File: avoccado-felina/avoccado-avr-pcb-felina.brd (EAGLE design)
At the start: 42.5 x 17.5 mm, 81 parts, among them Q1 16MHz, Q2 FET, U1 MPU-6000QFN-24, U2 MCP73831

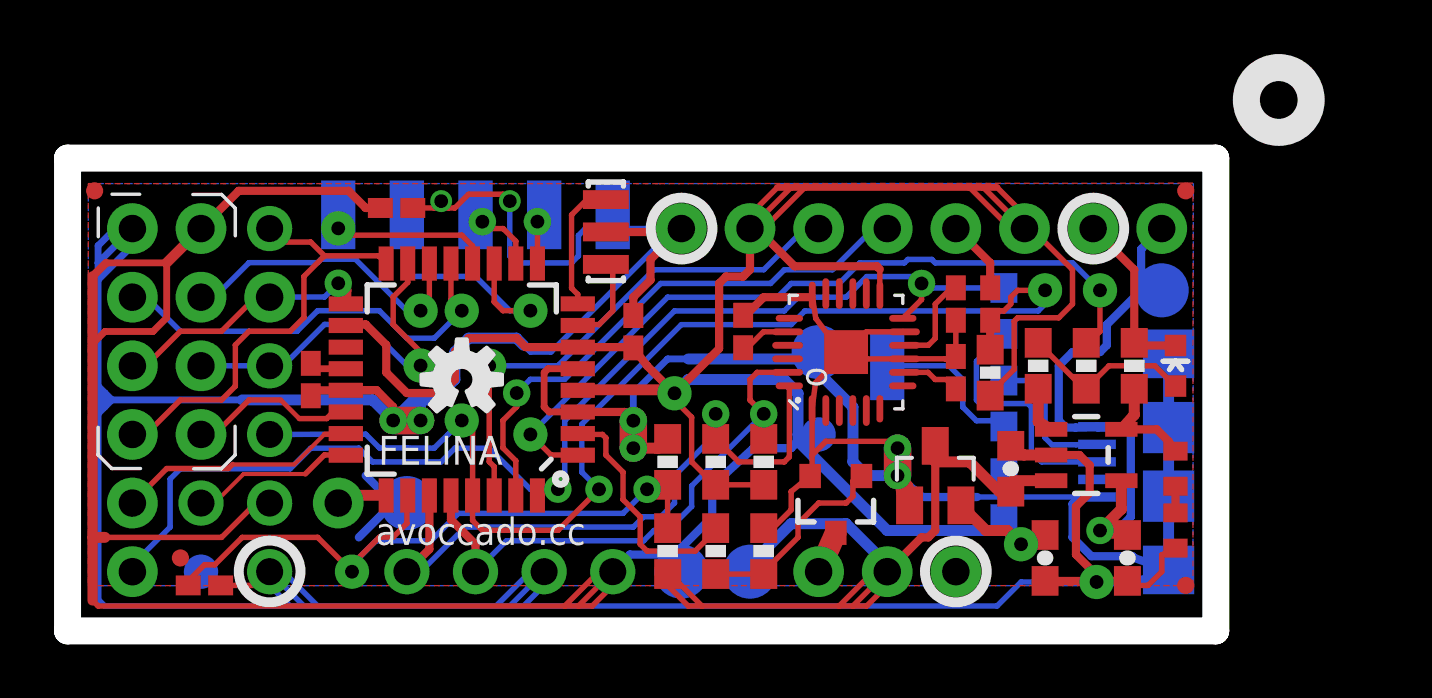
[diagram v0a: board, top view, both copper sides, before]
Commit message: rearrange board for panelization
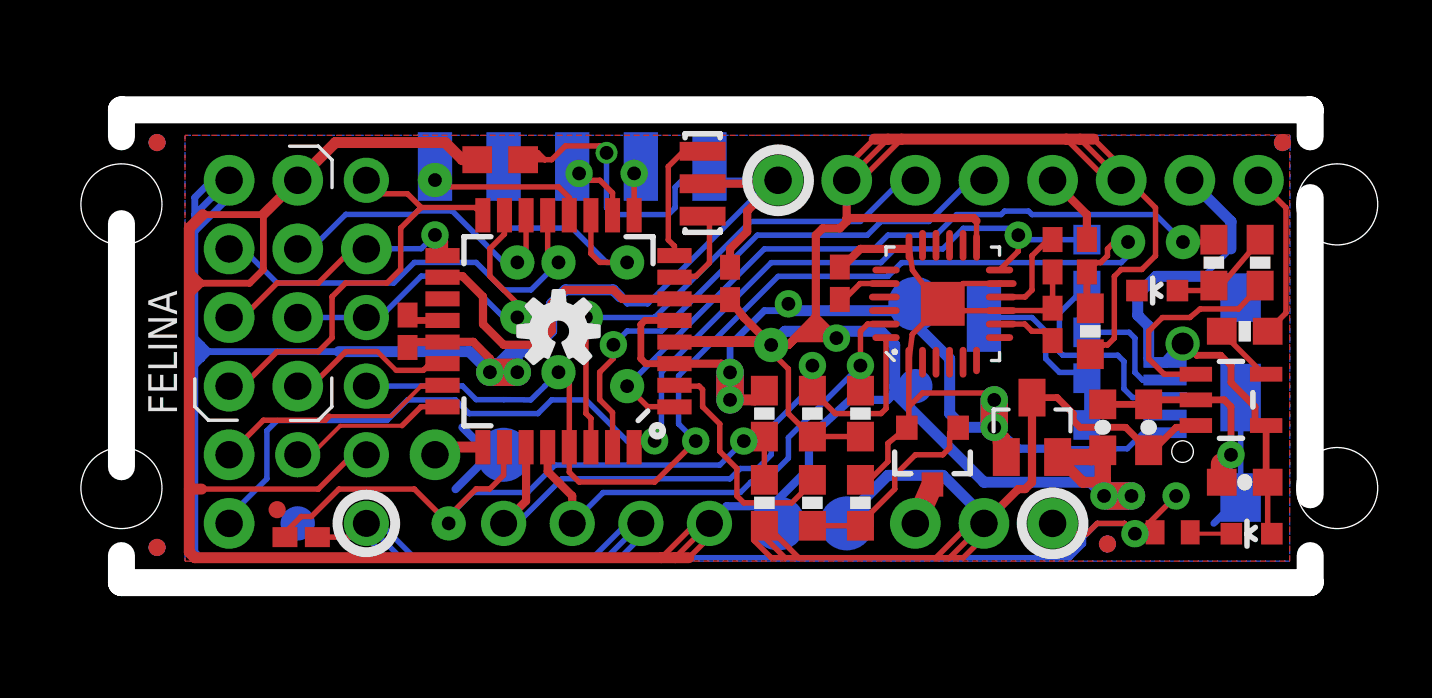
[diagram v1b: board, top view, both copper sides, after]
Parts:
- removed JP7: USB-MICROB, SparkFun-Connectors:USB-MICROB
- removed R12: 1K, rcl:R0402
- removed TP14: TPTP20R, testpad:TP20R
- added D2: LED, SparkFun:LED-0603
- added FID5, FID6, FID7, FID8, FID9: FIDUCIALUFIDUCIAL, SparkFun-Aesthetics:MICRO-FIDUCIAL
- added JP22: USB_MICROB_PLUGCONN-11752, SparkFun-Connectors:USB-B-MICRO-SMD_V03
- C10: device rcl:C0402K -> rcl:C0603
- R9: value 1K -> 2K
- moved FID4 38.1 mm to (2.82, 2.80)
- moved R4 9.06 mm to (43.6, 13.3)
- moved JP6 6.38 mm to (43.6, 16.4)
- moved R6 6.07 mm to (41.9, 13.3)
- moved U2 5.73 mm to (42.6, 8.26)
- moved C5 5.33 mm to (39.5, 7.25)
- moved C6 5.29 mm to (37.8, 7.25), turned to 90 degrees
- moved C4 5.17 mm to (43.1, 5.22), turned to 180 degrees
- moved R3 4.28 mm to (43.1, 10.8), turned to 180 degrees
- moved C10 4.23 mm to (15.5, 17.2)
- moved R2 4.01 mm to (37.4, 10.8)
- moved C8 4.00 mm to (36.0, 13.6)
- moved JP25 4.00 mm to (36.0, 3.69)
- moved C11 4.00 mm to (36.0, 11.1)
- moved JP10 4.00 mm to (36.0, 16.4)
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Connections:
- net 5V: now also D2.A, JP22.VBUS1; no longer JP7.VBUS, TP14.TP
- net CHG-PROG: no longer R12.2
- net GND: now also JP22.GND1, JP22.SHIELD1, JP22.SHIELD2, JP22.SHIELD3; no longer JP7.GND, JP7.MT1, JP7.MT2
- net N$3: now also D2.C; no longer R12.1
- net N$4: now also JP22.D+1; no longer JP7.D+
- net N$5: now also JP22.D-1; no longer JP7.D-
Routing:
- net GND: track 227.8 -> 212.2 mm, vias 9 -> 11
- net 3.3V: track 163.7 -> 173.8 mm, vias 2 -> 4
- net SOC: track 1.77 -> 7.83 mm
- net VBAT: track 32.8 -> 37.1 mm
- net LED: track 6.45 -> 4.26 mm
- net CHG-PROG: track 4.06 -> 2.44 mm
- net D3: track 28.6 -> 27.3 mm
- net N$4: track 9.25 -> 8.08 mm
- net N$5: track 5.40 -> 4.37 mm
- net RESET: track 43.0 -> 42.2 mm
- net A5: track 20.9 -> 20.2 mm
- net N$3: track 0.99 -> 1.54 mm
- net 7-TO-D-: track 7.57 -> 7.06 mm
- net D2-INT: track 43.6 -> 43.1 mm
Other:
- board size 42.5 x 17.5 mm -> 44 x 17.5 mm
- board text added: "AVOCCADO.CC"
- board text added: "DT"
- board text added: "G"
- board text added: "GN"
- board text added: "LIPO"
- board text added: "RX"
- board text added: "TX"
- board text removed: "BAT"
- board text removed: "D"
- board text removed: "R"
- board text removed: "T"
- board text removed: "avoccado.cc"
- board text removed: "o"

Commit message: Felina: remove screw mounts, Gin: prepare to panelize
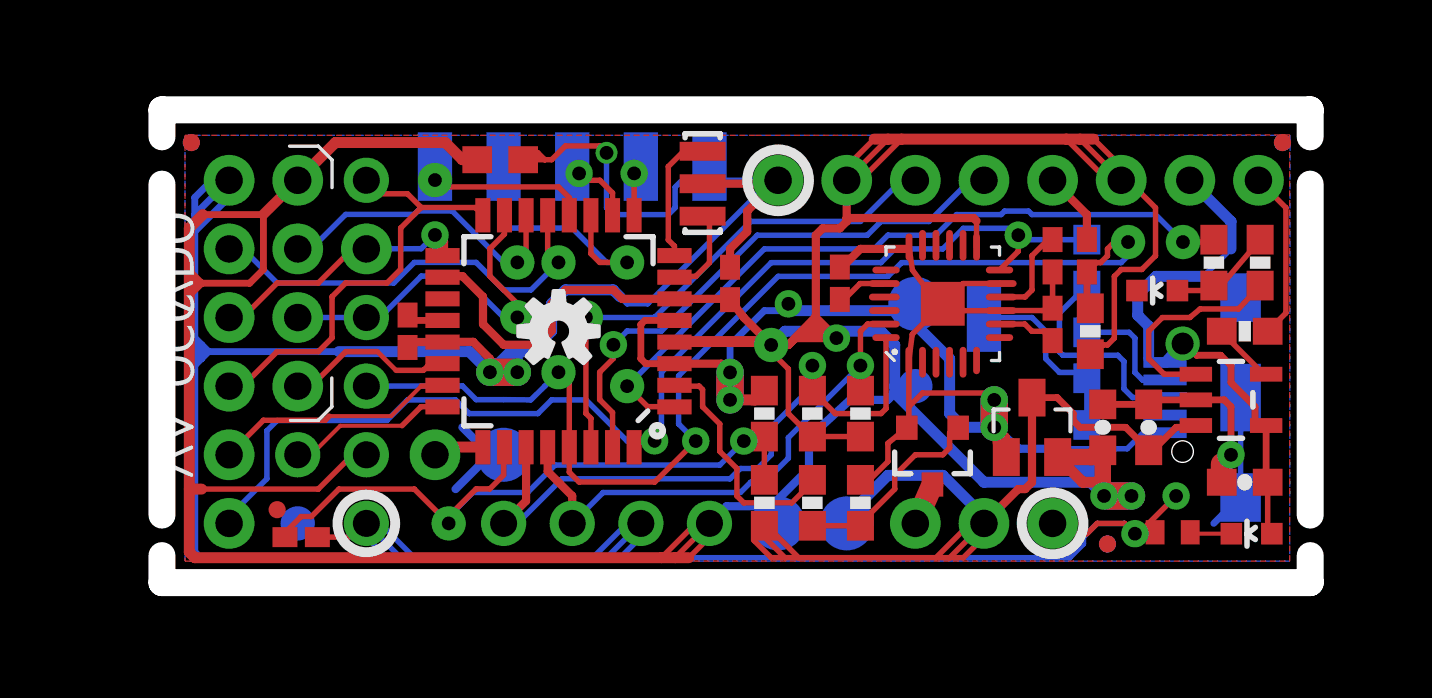
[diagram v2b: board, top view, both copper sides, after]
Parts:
- removed FID4, FID6: FIDUCIALUFIDUCIAL, SparkFun-Aesthetics:MICRO-FIDUCIAL
- moved FID1 1.27 mm to (4.09, 17.8)
- moved FID7 1.27 mm to (4.09, 17.8)
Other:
- board size 44 x 17.5 mm -> 42.5 x 17.5 mm
- board text added: "OCC DO"
- board text removed: "AVOCCADO.CC"
- board text removed: "FELINA"
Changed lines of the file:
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@@
 <setting verticaltext="up"/>
 </settings>
-<grid distance="0.02" unitdist="inch" unit="inch" style="lines" multiple="1" display="yes" altdistance="0.005" altunitdist="inch" altunit="inch"/>
+<grid distance="0.5" unitdist="mm" unit="mm" style="lines" multiple="1" display="yes" altdistance="0.1" altunitdist="mm" altunit="mm"/>
 <layers>
 <layer number="1" name="Top" color="47" fill="1" visible="yes" active="yes"/>
@@
 <description>Avoccado PCB AVR</description>
 <plain>
-<wire x1="5.787" y1="7.51" x2="4.723" y2="7.51" width="0.127" layer="21"/>
-<wire x1="4.723" y1="7.51" x2="4.215" y2="8.018" width="0.127" layer="21"/>
-<wire x1="4.215" y1="8.018" x2="4.215" y2="9.042" width="0.127" layer="21"/>
 <text x="36.560371875" y="6.393159375" size="1.778" layer="22" font="vector" ratio="15" rot="MR0" align="top-left">-</text>
 <text x="14.248" y="9.699" size="1.27" layer="22" ratio="15" rot="SMR0" align="center-left">RS</text>
@@
 <text x="34.018759375" y="6.433603125" size="1.778" layer="22" font="vector" ratio="15" rot="MR0" align="top-left">+</text>
 <text x="39.361" y="14.868" size="1.016" layer="22" ratio="15" rot="SMR0" align="top-left">VC</text>
-<text x="2.491" y="7.718" size="1.0668" layer="21" ratio="15" rot="R90" align="top-left">FELINA</text>
-<wire x1="1.5" y1="14.787" x2="1.5" y2="5.787" width="1" layer="46"/>
-<wire x1="1.5" y1="2.5" x2="1.5" y2="1.5" width="1" layer="46"/>
-<wire x1="1.5" y1="1.5" x2="45.5" y2="1.5" width="1" layer="46"/>
+<wire x1="3" y1="16.25" x2="3" y2="4" width="1" layer="46"/>
+<wire x1="3" y1="2.5" x2="3" y2="1.5" width="1" layer="46"/>
+<wire x1="3" y1="1.5" x2="45.5" y2="1.5" width="1" layer="46"/>
 <wire x1="45.5" y1="1.5" x2="45.5" y2="2.5" width="1" layer="46"/>
 <text x="41.901" y="14.868" size="1.016" layer="22" ratio="15" rot="SMR0" align="top-left">5V</text>
@@
 <circle x="44.474" y="17.789" radius="0.254" width="0.6096" layer="29"/>
 <circle x="7.263" y="4.2" radius="0.254" width="0.6096" layer="29"/>
-<circle x="2.818" y="17.789" radius="0.254" width="0.6096" layer="29"/>
-<hole x="1.5" y="5" drill="3"/>
-<hole x="1.5" y="15.5" drill="3"/>
+<circle x="4.088" y="17.789" radius="0.254" width="0.6096" layer="29"/>
 <wire x1="45.5" y1="18" x2="45.5" y2="19" width="1" layer="46"/>
-<wire x1="45.5" y1="19" x2="1.5" y2="19" width="1" layer="46"/>
-<wire x1="1.5" y1="19" x2="1.5" y2="18" width="1" layer="46"/>
-<wire x1="45.5" y1="4.75" x2="45.5" y2="15.75" width="1" layer="46"/>
+<wire x1="45.5" y1="19" x2="3" y2="19" width="1" layer="46"/>
+<wire x1="3" y1="19" x2="3" y2="18" width="1" layer="46"/>
+<wire x1="45.5" y1="4" x2="45.5" y2="16.25" width="1" layer="46"/>
 <wire x1="11.454" y1="15.724" x2="11.962" y2="15.216" width="0.254" layer="22"/>
 <wire x1="11.454" y1="13.184" x2="11.962" y2="12.676" width="0.254" layer="22"/>
@@
 <wire x1="34.822" y1="7.883" x2="34.822" y2="7.756" width="0.1524" layer="22"/>
 <circle x="15.645" y="6.24" radius="1.1" width="0.2032" layer="22"/>
-<circle x="2.818" y="2.803" radius="0.254" width="0.6096" layer="29"/>
 <circle x="37.997" y="2.93" radius="0.254" width="0.6096" layer="29"/>
-<circle x="2.818" y="17.789" radius="0.254" width="0.6096" layer="30"/>
-<circle x="2.818" y="2.803" radius="0.254" width="0.6096" layer="30"/>
+<circle x="4.088" y="17.789" radius="0.254" width="0.6096" layer="30"/>
 <circle x="37.997" y="2.93" radius="0.254" width="0.6096" layer="30"/>
 <circle x="44.474" y="17.789" radius="0.254" width="0.6096" layer="30"/>
-<hole x="46.5" y="15.5" drill="3"/>
-<hole x="46.5" y="5" drill="3"/>
-<text x="4.209" y="5.318" size="1.0668" layer="22" ratio="15" rot="MR90" align="top-left">AVOCCADO.CC</text>
-<polygon width="0.05" layer="22">
-<vertex x="29.5" y="3"/>
-<vertex x="24.5" y="15"/>
-<vertex x="22" y="15"/>
-<vertex x="17" y="3"/>
-<vertex x="19" y="3"/>
-<vertex x="23.25" y="13.75"/>
-<vertex x="27.5" y="3"/>
-</polygon>
-<circle x="20.008" y="15.008" radius="0.9" width="0.8128" layer="22"/>
 <circle x="8.025" y="3.7" radius="0.762" width="0.2" layer="22"/>
 <circle x="25.805" y="16.4" radius="1.0668" width="0.2" layer="22"/>
@@
 <wire x1="16.51" y1="14.986" x2="16.51" y2="12.7" width="0.254" layer="22"/>
 <text x="19.496" y="12.872" size="1.27" layer="22" ratio="15" rot="SMR0" align="center-left">G</text>
+<text x="4.1783" y="15.2527" size="1.3081" layer="21" ratio="12" rot="R270" align="top-left">OCC DO</text>
+<polygon width="0.05" layer="22">
+<vertex x="16.2186" y="3.9816"/>
+<vertex x="21.7266" y="17.5056"/>
+<vertex x="23.2106" y="17.5056"/>
+<vertex x="28.7186" y="3.9816"/>
+<vertex x="26.7186" y="3.9816"/>
+<vertex x="22.4686" y="14.7316"/>
+<vertex x="18.2186" y="3.9816"/>
+</polygon>
+<circle x="18.3687625" y="15.836528125" radius="1.27" width="1.27" layer="22"/>
+<wire x1="4.0894" y1="11.5824" x2="2.9464" y2="12.0904" width="0.1524" layer="21"/>
+<wire x1="2.9464" y1="12.0904" x2="4.0894" y2="12.5984" width="0.1524" layer="21"/>
+<wire x1="2.9464" y1="7.7724" x2="4.0894" y2="7.2644" width="0.1524" layer="21"/>
+<wire x1="4.0894" y1="7.2644" x2="2.9464" y2="6.7564" width="0.1524" layer="21"/>
+<wire x1="4.0894" y1="5.4864" x2="2.9464" y2="5.9944" width="0.1524" layer="21"/>
+<wire x1="2.9464" y1="5.9944" x2="4.0894" y2="6.5024" width="0.1524" layer="21"/>
+<circle x="2.8194" y="15.2654" radius="0.127" width="0.1524" layer="21"/>
 </plain>
 <attributes>
@@
 <element name="FID2" library="SparkFun-Aesthetics" package="MICRO-FIDUCIAL" value="FIDUCIALUFIDUCIAL" x="44.474" y="17.789"/>
 <element name="LOGO1" library="SparkFun-Aesthetics" package="OSHW-LOGO-S" value="OSHW-LOGOS" x="17.677" y="10.804"/>
-<element name="FID1" library="SparkFun-Aesthetics" package="MICRO-FIDUCIAL" value="FIDUCIALUFIDUCIAL" x="2.818" y="17.789"/>
+<element name="FID1" library="SparkFun-Aesthetics" package="MICRO-FIDUCIAL" value="FIDUCIALUFIDUCIAL" x="4.088" y="17.789"/>
 <element name="FID3" library="SparkFun-Aesthetics" package="MICRO-FIDUCIAL" value="FIDUCIALUFIDUCIAL" x="7.263" y="4.2"/>
 <element name="JP22" library="SparkFun-Connectors" package="USB-B-MICRO-SMD_V03" value="USB_MICROB_PLUGCONN-11752" x="42.926" y="8.35" smashed="yes" rot="MR0">
@@
 <attribute name="VALUE" x="41.299" y="4.1492" size="0.4064" layer="27" rot="R180"/>
 </element>
-<element name="FID4" library="SparkFun-Aesthetics" package="MICRO-FIDUCIAL" value="FIDUCIALUFIDUCIAL" x="2.818" y="2.803"/>
 <element name="FID5" library="SparkFun-Aesthetics" package="MICRO-FIDUCIAL" value="FIDUCIALUFIDUCIAL" x="37.997" y="2.93"/>
-<element name="FID6" library="SparkFun-Aesthetics" package="MICRO-FIDUCIAL" value="FIDUCIALUFIDUCIAL" x="2.818" y="2.803" rot="MR0"/>
-<element name="FID7" library="SparkFun-Aesthetics" package="MICRO-FIDUCIAL" value="FIDUCIALUFIDUCIAL" x="2.818" y="17.789" rot="MR0"/>
+<element name="FID7" library="SparkFun-Aesthetics" package="MICRO-FIDUCIAL" value="FIDUCIALUFIDUCIAL" x="4.088" y="17.789" rot="MR0"/>
 <element name="FID8" library="SparkFun-Aesthetics" package="MICRO-FIDUCIAL" value="FIDUCIALUFIDUCIAL" x="44.474" y="17.789" rot="MR0"/>
 <element name="FID9" library="SparkFun-Aesthetics" package="MICRO-FIDUCIAL" value="FIDUCIALUFIDUCIAL" x="37.997" y="2.93" rot="MR0"/>
